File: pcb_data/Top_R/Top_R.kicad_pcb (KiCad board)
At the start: 2 copper layers, 163.1 x 96.4 mm, 46 parts

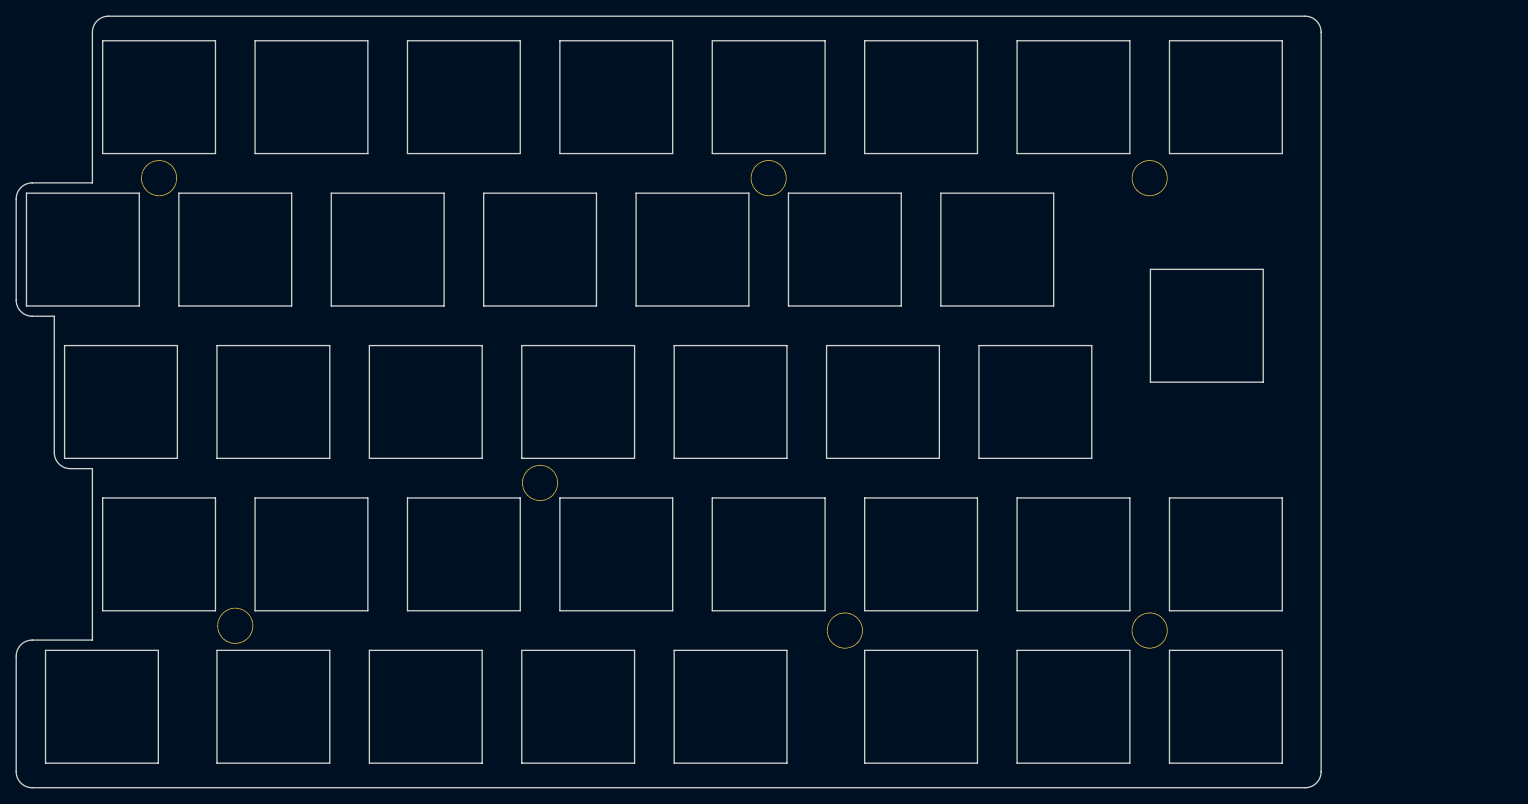
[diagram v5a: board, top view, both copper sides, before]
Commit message: fix hole footprint and number
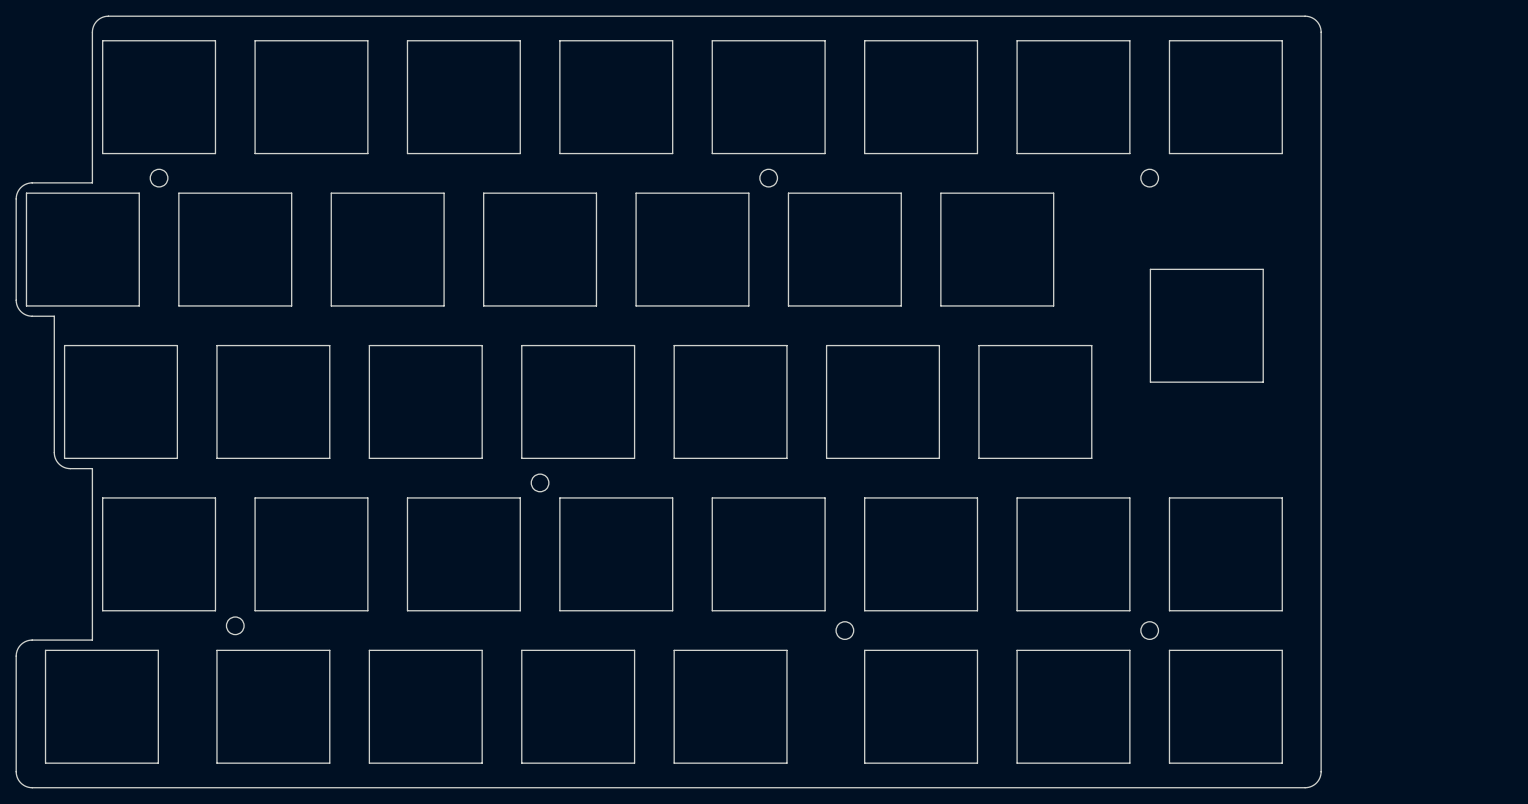
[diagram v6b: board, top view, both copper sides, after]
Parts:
- H1, H2, H3, H4, H5, H6: footprint kbd_Hole:m2_Spacer_Hole -> kbd_Hole:m2_Screw_Hole
- H7: renamed from H8; footprint kbd_Hole:m2_Spacer_Hole -> kbd_Hole:m2_Screw_Hole
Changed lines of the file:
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@@
 		(embedded_fonts no)
 	)
-	(footprint "kbd_Hole:m2_Spacer_Hole"
+	(footprint "kbd_Hole:m2_Screw_Hole"
 		(layer "F.Cu")
 		(at 207.168924 67.270369)
@@
 			)
 		)
-		(property "Datasheet" "~"
+		(property "Datasheet" ""
 			(at 0 0 0)
 			(layer "F.Fab")
@@
 			)
 		)
-		(property "Description" "Mounting Hole without connection"
+		(property "Description" ""
 			(at 0 0 0)
 			(layer "F.Fab")
@@
 		(fp_circle
 			(center 0 0)
-			(end 2.3 0)
+			(end 2.45 0)
 			(stroke
 				(width 0.05)
@@
 		(pad "" np_thru_hole circle
 			(at 0 0)
-			(size 4.5 4.5)
-			(drill 4.3)
+			(size 2.2 2.2)
+			(drill 2.2)
 			(layers "*.Cu" "*.Mask")
 		)
@@
 		(embedded_fonts no)
 	)
-	(footprint "kbd_Hole:m2_Spacer_Hole"
+	(footprint "kbd_Hole:m2_Screw_Hole"
 		(layer "F.Cu")
 		(at 207.168924 123.825104)
@@
 			)
 		)
-		(property "Datasheet" "~"
+		(property "Datasheet" ""
 			(at 0 0 0)
 			(layer "F.Fab")
@@
 			)
 		)
-		(property "Description" "Mounting Hole without connection"
+		(property "Description" ""
 			(at 0 0 0)
 			(layer "F.Fab")
@@
 		(fp_circle
 			(center 0 0)
-			(end 2.3 0)
+			(end 2.45 0)
 			(stroke
 				(width 0.05)
@@
 		(pad "" np_thru_hole circle
 			(at 0 0)
-			(size 4.5 4.5)
-			(drill 4.3)
+			(size 2.2 2.2)
+			(drill 2.2)
 			(layers "*.Cu" "*.Mask")
 		)
@@
 		(embedded_fonts no)
 	)
-	(footprint "kbd_Hole:m2_Spacer_Hole"
+	(footprint "kbd_Hole:m2_Screw_Hole"
 		(layer "F.Cu")
 		(at 130.96886 105.370401)
 		(descr "Mounting Hole 2.2mm, no annular, M2")
 		(tags "mounting hole 2.2mm no annular m2")
-		(property "Reference" "H8"
+		(property "Reference" "H7"
 			(at 0 -3.2 0)
 			(layer "F.Fab")
@@
 			)
 		)
-		(property "Datasheet" "~"
+		(property "Datasheet" ""
 			(at 0 0 0)
 			(layer "F.Fab")
@@
 			)
 		)
-		(property "Description" "Mounting Hole without connection"
+		(property "Description" ""
 			(at 0 0 0)
 			(layer "F.Fab")
@@
 		(fp_circle
 			(center 0 0)
-			(end 2.3 0)
+			(end 2.45 0)
 			(stroke
 				(width 0.05)
@@
 		(pad "" np_thru_hole circle
 			(at 0 0)
-			(size 4.5 4.5)
-			(drill 4.3)
+			(size 2.2 2.2)
+			(drill 2.2)
 			(layers "*.Cu" "*.Mask")
 		)
@@
 		(embedded_fonts no)
 	)
-	(footprint "kbd_Hole:m2_Spacer_Hole"
+	(footprint "kbd_Hole:m2_Screw_Hole"
 		(layer "F.Cu")
 		(at 83.34382 67.270369)
@@
 			)
 		)
-		(property "Datasheet" "~"
+		(property "Datasheet" ""
 			(at 0 0 0)
 			(layer "F.Fab")
@@
 			)
 		)
-		(property "Description" "Mounting Hole without connection"
+		(property "Description" ""
 			(at 0 0 0)
 			(layer "F.Fab")
@@
 		(fp_circle
 			(center 0 0)
-			(end 2.3 0)
+			(end 2.45 0)
 			(stroke
 				(width 0.05)
@@
 		(pad "" np_thru_hole circle
 			(at 0 0)
-			(size 4.5 4.5)
-			(drill 4.3)
+			(size 2.2 2.2)
+			(drill 2.2)
 			(layers "*.Cu" "*.Mask")
 		)
@@
 		(embedded_fonts no)
 	)
-	(footprint "kbd_Hole:m2_Spacer_Hole"
+	(footprint "kbd_Hole:m2_Screw_Hole"
 		(layer "F.Cu")
 		(at 159.543884 67.270369)
@@
 			)
 		)
-		(property "Datasheet" "~"
+		(property "Datasheet" ""
 			(at 0 0 0)
 			(layer "F.Fab")
@@
 			)
 		)
-		(property "Description" "Mounting Hole without connection"
+		(property "Description" ""
 			(at 0 0 0)
 			(layer "F.Fab")
@@
 		(fp_circle
 			(center 0 0)
-			(end 2.3 0)
+			(end 2.45 0)
 			(stroke
 				(width 0.05)
@@
 		(pad "" np_thru_hole circle
 			(at 0 0)
-			(size 4.5 4.5)
-			(drill 4.3)
+			(size 2.2 2.2)
+			(drill 2.2)
 			(layers "*.Cu" "*.Mask")
 		)
 		(embedded_fonts no)
 	)
-	(footprint "kbd_Hole:m2_Spacer_Hole"
+	(footprint "kbd_Hole:m2_Screw_Hole"
 		(layer "F.Cu")
 		(at 92.868828 123.229791)
@@
 			)
 		)
-		(property "Datasheet" "~"
+		(property "Datasheet" ""
 			(at 0 0 0)
 			(layer "F.Fab")
@@
 			)
 		)
-		(property "Description" "Mounting Hole without connection"
+		(property "Description" ""
 			(at 0 0 0)
 			(layer "F.Fab")
@@
 		(fp_circle
 			(center 0 0)
-			(end 2.3 0)
+			(end 2.45 0)
 			(stroke
 				(width 0.05)
@@
 		(pad "" np_thru_hole circle
 			(at 0 0)
-			(size 4.5 4.5)
-			(drill 4.3)
+			(size 2.2 2.2)
+			(drill 2.2)
 			(layers "*.Cu" "*.Mask")
 		)
@@
 		(embedded_fonts no)
 	)
-	(footprint "kbd_Hole:m2_Spacer_Hole"
+	(footprint "kbd_Hole:m2_Screw_Hole"
 		(layer "F.Cu")
 		(at 169.068892 123.825104)
@@
 			)
 		)
-		(property "Datasheet" "~"
+		(property "Datasheet" ""
 			(at 0 0 0)
 			(layer "F.Fab")
@@
 			)
 		)
-		(property "Description" "Mounting Hole without connection"
+		(property "Description" ""
 			(at 0 0 0)
 			(layer "F.Fab")
@@
 		(fp_circle
 			(center 0 0)
-			(end 2.3 0)
+			(end 2.45 0)
 			(stroke
 				(width 0.05)
@@
 		(pad "" np_thru_hole circle
 			(at 0 0)
-			(size 4.5 4.5)
-			(drill 4.3)
+			(size 2.2 2.2)
+			(drill 2.2)
 			(layers "*.Cu" "*.Mask")
 		)
